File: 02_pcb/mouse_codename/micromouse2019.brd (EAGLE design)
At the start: 45 x 50 mm, 77 parts

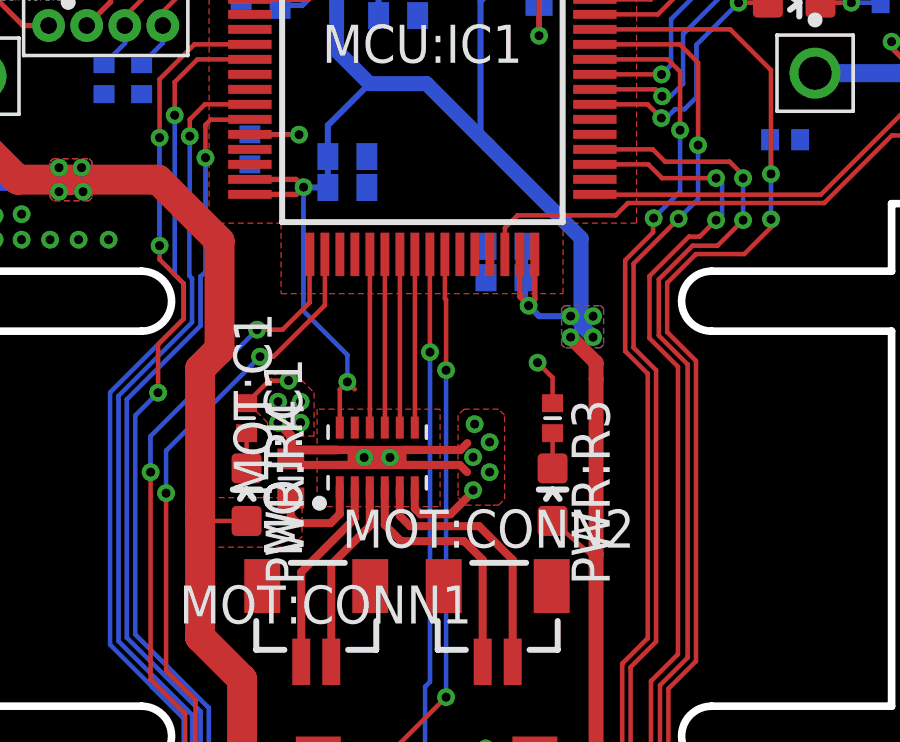
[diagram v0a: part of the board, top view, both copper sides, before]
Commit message: mot drv wire stub removed
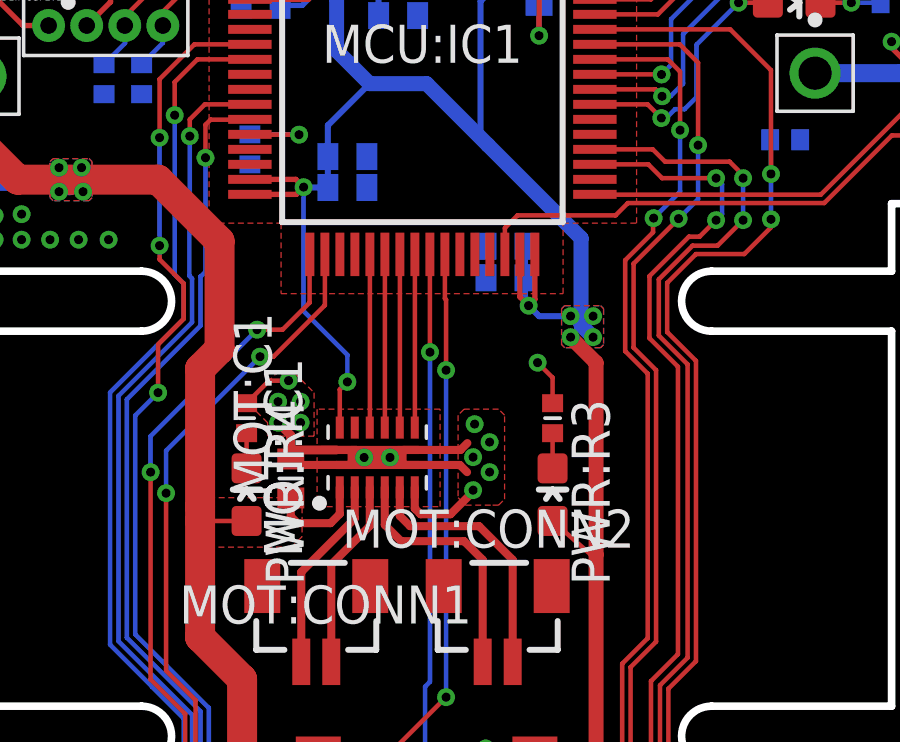
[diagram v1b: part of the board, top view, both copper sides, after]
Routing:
- net +3V3: track 165.8 -> 165.2 mm
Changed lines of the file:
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@@
 <drawing>
 <settings>
-<setting alwaysvectorfont="yes"/>
+<setting alwaysvectorfont="no"/>
 <setting verticaltext="up"/>
 </settings>
@@
 <contactref element="EPL:PORT1" pad="P3"/>
 <contactref element="PWR:LDO1" pad="1"/>
-<wire x1="20.106" y1="23.814" x2="19.86" y2="24.06" width="0.1524" layer="1"/>
 <wire x1="19.606" y1="22.5356" x2="19.606" y2="23.806" width="0.1524" layer="1"/>
 <wire x1="19.606" y1="23.806" x2="19.86" y2="24.06" width="0.1524" layer="1"/>
@@
 <wire x1="38.19" y1="4.73" x2="38.19" y2="3.71" width="0.1524" layer="16"/>
 <wire x1="38.19" y1="3.71" x2="38.2" y2="3.7" width="0.1524" layer="16"/>
-<wire x1="28.15" y1="18.3" x2="28.15" y2="24.15" width="0.5" layer="1"/>
+<wire x1="28.15" y1="18.3" x2="28.15" y2="24.7" width="0.5" layer="1"/>
 <wire x1="19.86" y1="24.06" x2="19.86" y2="24.96" width="0.1524" layer="16"/>
 <wire x1="19.86" y1="24.96" x2="18.4" y2="26.42" width="0.1524" layer="16"/>
@@
 <wire x1="16.61" y1="30.81" x2="18.14" y2="30.81" width="0.1778" layer="1"/>
 <wire x1="18.14" y1="30.81" x2="18.25" y2="30.7" width="0.1778" layer="1"/>
-<wire x1="18.25" y1="30.7" x2="18.4" y2="30.55" width="0.1778" layer="1"/>
 <wire x1="18.4" y1="26.42" x2="18.4" y2="30.55" width="0.1524" layer="16"/>
 <wire x1="18.4" y1="30.55" x2="18.25" y2="30.7" width="0.1778" layer="1"/>
@@
 </polygon>
 <wire x1="28.15" y1="24.7" x2="27.3" y2="25.55" width="0.5" layer="1"/>
-<wire x1="28.15" y1="24.15" x2="28.15" y2="24.7" width="0.5" layer="1"/>
 <wire x1="28.05" y1="25.55" x2="27.65" y2="25.95" width="0.5" layer="16"/>
 <wire x1="22.5" y1="34" x2="20.6" y2="34" width="0.5" layer="16"/>
@@
 <wire x1="18.773" y1="46.177" x2="18.773" y2="46.225" width="0.127" layer="16"/>
 <wire x1="18.773" y1="46.225" x2="18.775" y2="46.225" width="0.127" layer="16"/>
+<wire x1="27.65" y1="25.95" x2="28.05" y2="26.25" width="0" layer="19" extent="16-16"/>
+<wire x1="27.3" y1="26.25" x2="27.65" y2="25.95" width="0" layer="19" extent="16-16"/>
+<wire x1="27.3" y1="25.55" x2="27.65" y2="25.95" width="0" layer="19" extent="16-16"/>
 </signal>
 <signal name="VCC">

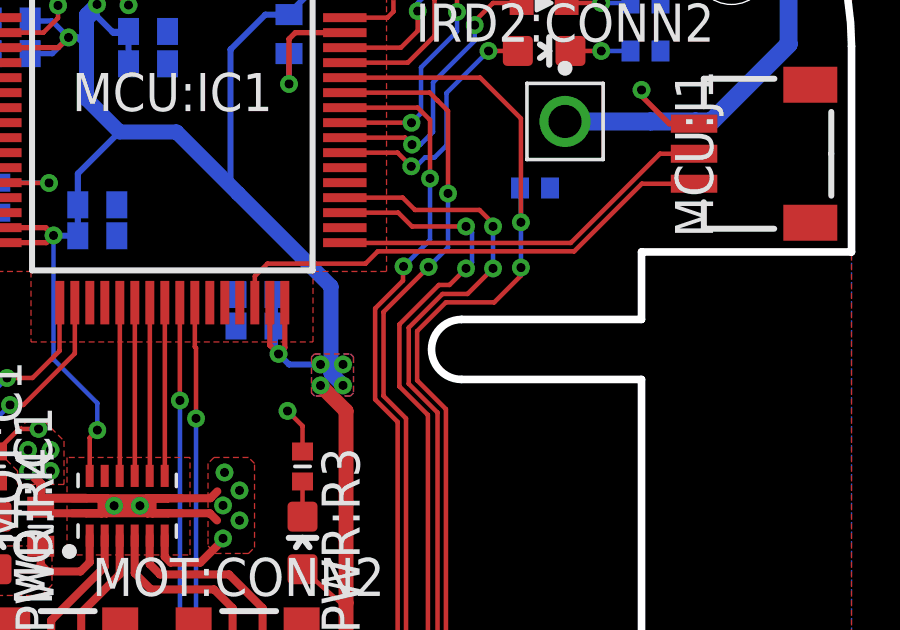
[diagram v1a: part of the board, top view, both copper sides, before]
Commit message: 100k resistor added to SWDIO for bidirectional managment
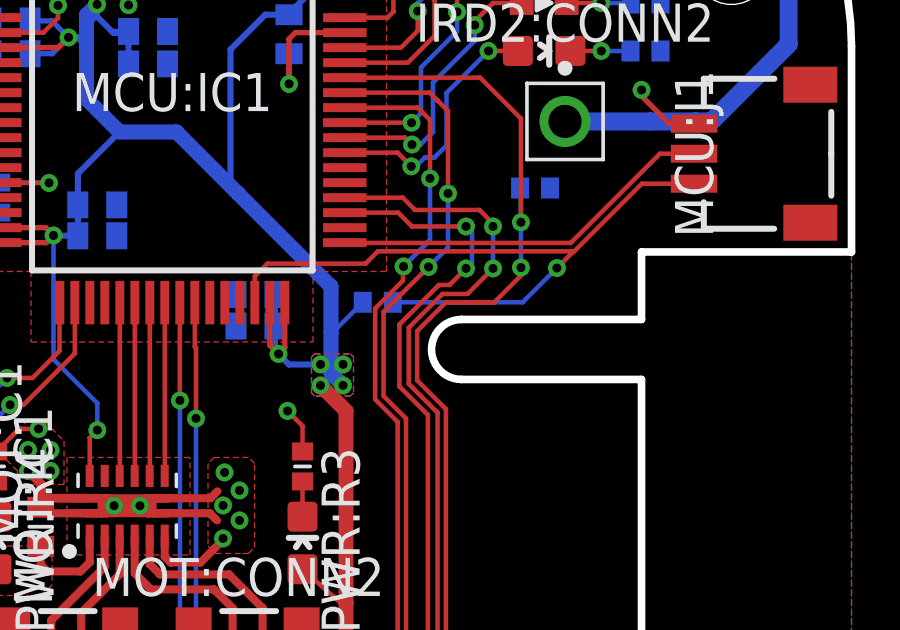
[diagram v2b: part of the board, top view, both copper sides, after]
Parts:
- added MCU:R10: 100k, rcl:R0402
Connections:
- net +3V3: now also MCU:R10.2
- net MCU:SWDIO: now also MCU:R10.1
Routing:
- net MCU:SWDIO: track 16.8 -> 23.5 mm, vias 0 -> 1
- net +3V3: track 165.2 -> 166.7 mm
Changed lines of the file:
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@@
 <attribute name="VALUE" x="20.701" y="-0.254" size="1.27" layer="27" align="top-center"/>
+</element>
+<element name="MCU:R10" library="rcl" library_urn="urn:adsk.eagle:library:334" package="R0402" package3d_urn="urn:adsk.eagle:package:23547/3" value="100k" x="29.21" y="28.321" smashed="yes" rot="MR0">
+<attribute name="NAME" x="29.845" y="28.956" size="1.27" layer="26" rot="MR0"/>
+<attribute name="SPICEPREFIX" value="R" x="29.21" y="28.321" size="1.778" layer="28" rot="MR0" display="off"/>
+<attribute name="VALUE" x="29.845" y="26.416" size="1.27" layer="28" rot="MR0"/>
 </element>
 </elements>
@@
 <wire x1="25.11" y1="29.19" x2="25.11" y2="28.31" width="0.1524" layer="1"/>
 <contactref element="MCU:IC1" pad="46"/>
+<contactref element="MCU:R10" pad="1"/>
+<wire x1="29.71" y1="28.321" x2="34.036" y2="28.321" width="0.1524" layer="16"/>
+<via x="35.179" y="29.464" extent="1-16" drill="0.3" diameter="0.6"/>
+<wire x1="35.179" y1="29.464" x2="35.7356" y2="30.0206" width="0.1524" layer="1"/>
+<wire x1="35.7356" y1="30.0206" x2="35.7557375" y2="30.0206" width="0.1524" layer="1"/>
+<wire x1="34.036" y1="28.321" x2="35.179" y2="29.464" width="0.1524" layer="16"/>
 </signal>
 <signal name="MCU:SWCLK">
@@
 <contactref element="CONN1" pad="1"/>
 <contactref element="CONN2" pad="1"/>
+<wire x1="26.25" y1="37.1" x2="22.2" y2="37.35" width="0" layer="19" extent="1-16"/>
 </signal>
 <signal name="+3V3">
@@
 <wire x1="22.5" y1="34" x2="20.6" y2="34" width="0.5" layer="16"/>
 <wire x1="20.6" y1="34" x2="19.5" y2="35.1" width="0.5" layer="16"/>
-<wire x1="27.65" y1="25.95" x2="27.65" y2="28.85" width="0.5" layer="16"/>
+<wire x1="27.65" y1="25.95" x2="27.65" y2="27.305" width="0.5" layer="16"/>
+<wire x1="27.65" y1="27.305" x2="27.65" y2="28.85" width="0.5" layer="16"/>
 <wire x1="27.65" y1="28.85" x2="24.55" y2="31.95" width="0.5" layer="16"/>
 <wire x1="24.55" y1="31.95" x2="22.5" y2="34" width="0.5" layer="16"/>
@@
 <wire x1="18.773" y1="46.177" x2="18.773" y2="46.225" width="0.127" layer="16"/>
 <wire x1="18.773" y1="46.225" x2="18.775" y2="46.225" width="0.127" layer="16"/>
-<wire x1="27.65" y1="25.95" x2="28.05" y2="26.25" width="0" layer="19" extent="16-16"/>
-<wire x1="27.3" y1="26.25" x2="27.65" y2="25.95" width="0" layer="19" extent="16-16"/>
-<wire x1="27.3" y1="25.55" x2="27.65" y2="25.95" width="0" layer="19" extent="16-16"/>
+<contactref element="MCU:R10" pad="2"/>
+<wire x1="28.71" y1="28.321" x2="27.694" y2="27.305" width="0.1524" layer="16"/>
+<wire x1="27.694" y1="27.305" x2="27.65" y2="27.305" width="0.1524" layer="16"/>
 </signal>
 <signal name="VCC">

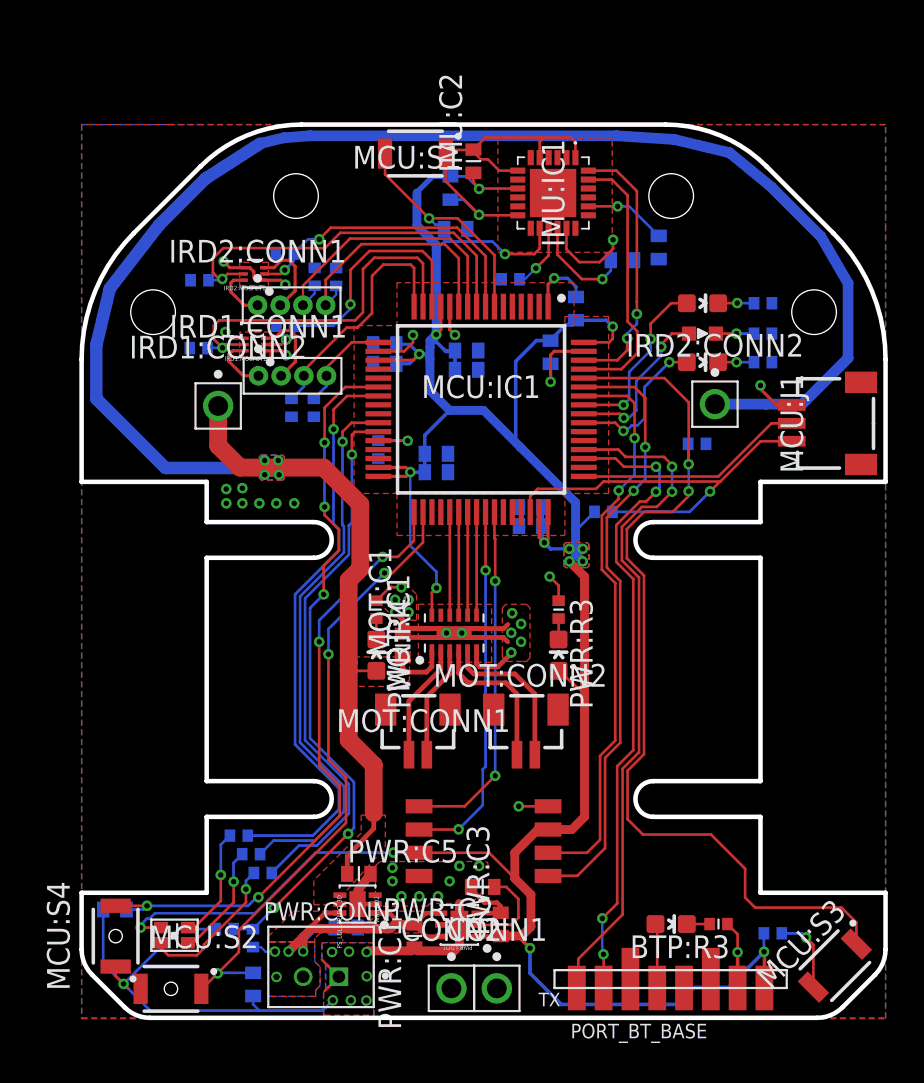
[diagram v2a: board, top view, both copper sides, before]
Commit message: tNames sized and placed to position
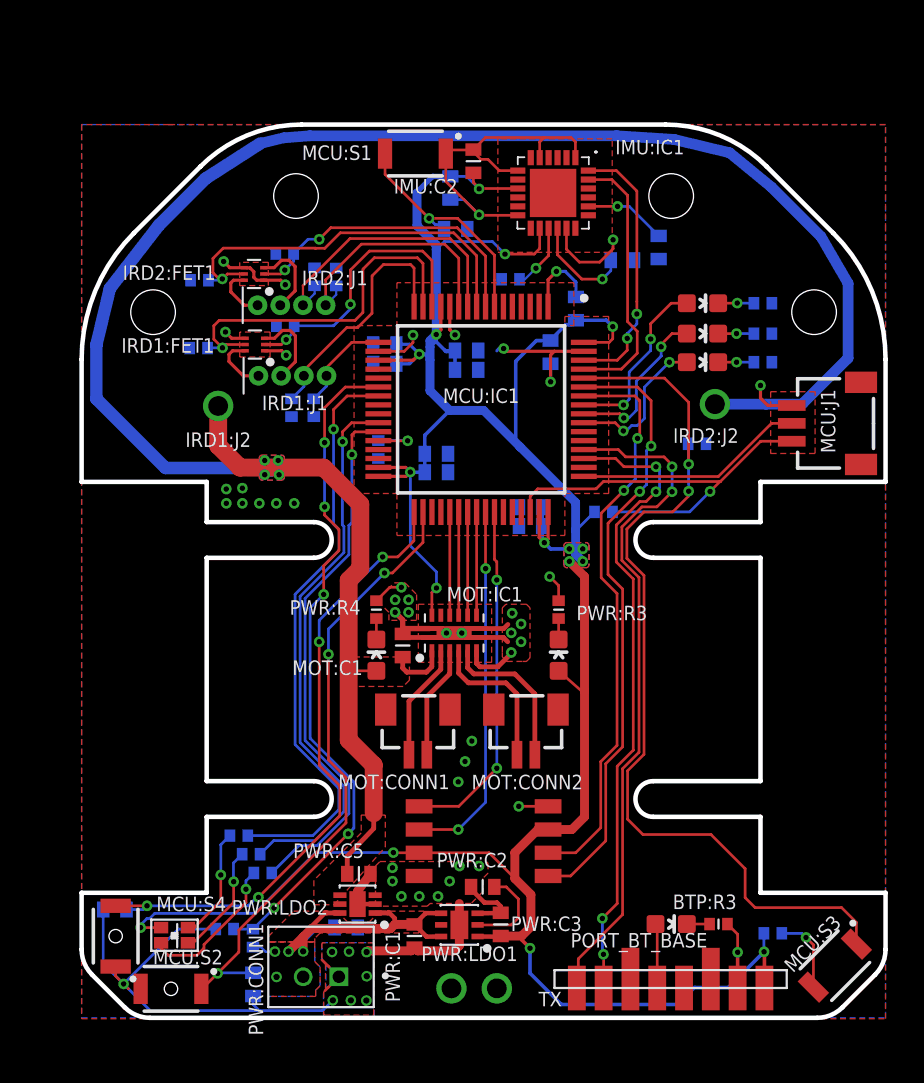
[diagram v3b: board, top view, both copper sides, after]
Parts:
- renumbered IRD1:CONN1 to IRD1:J1, IRD1:CONN2 to IRD1:J2, IRD1:MOSFET1 to IRD1:FET1, IRD2:CONN1 to IRD2:J1, IRD2:CONN2 to IRD2:J2, IRD2:MOSFET1 to IRD2:FET1
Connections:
- net ENC_LEFT_CHA: now also EPL:PORT1.P1, MCU:IC1.42; no longer EPL:PORT1.P2, MCU:IC1.41
- net ENC_LEFT_CHB: now also EPL:PORT1.P2, MCU:IC1.41; no longer EPL:PORT1.P1, MCU:IC1.42
- net ENC_RIGHT_CHA: now also EPR:PORT1.P1, MCU:IC1.59; no longer EPR:PORT1.P2, MCU:IC1.58
- net ENC_RIGHT_CHB: now also EPR:PORT1.P2, MCU:IC1.58; no longer EPR:PORT1.P1, MCU:IC1.59
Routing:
- net GND: track 119.8 -> 123.5 mm, vias 48 -> 52
- net ENC_RIGHT_CHA: track 32.1 -> 34.5 mm
- net ENC_RIGHT_CHB: track 34.3 -> 32.3 mm
- net ENC_LEFT_CHA: track 20.6 -> 19.6 mm
- net ENC_LEFT_CHB: track 19.7 -> 20.6 mm
- net MCU:V_BAT: track 3.73 -> 4.34 mm

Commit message: drc rule check ok
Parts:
- MCU:R1, MCU:R10: device rcl:R0402 -> 0-micromouse2019:R0402
- moved PWR:R1 1.06 mm to (8.56, 4.20)
- moved PWR:R2 1.05 mm to (6.99, 4.72)
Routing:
- net GND: track 123.5 -> 119.5 mm
- net V_BAT_LEVEL: track 38.1 -> 39.3 mm
- net PWR:V_BAT_IN: track 19.7 -> 20.6 mm

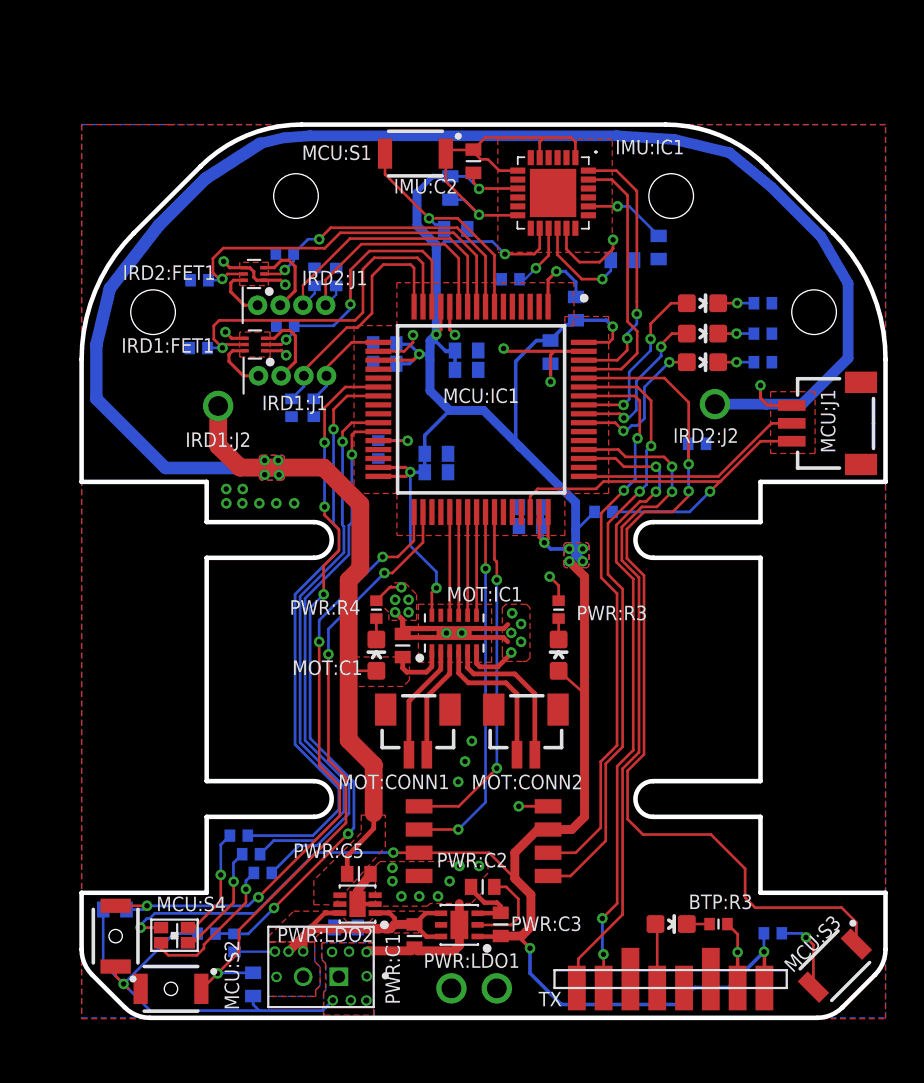
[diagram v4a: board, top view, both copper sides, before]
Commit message: FET thermal ground added & LDOs & FET variant names corrected
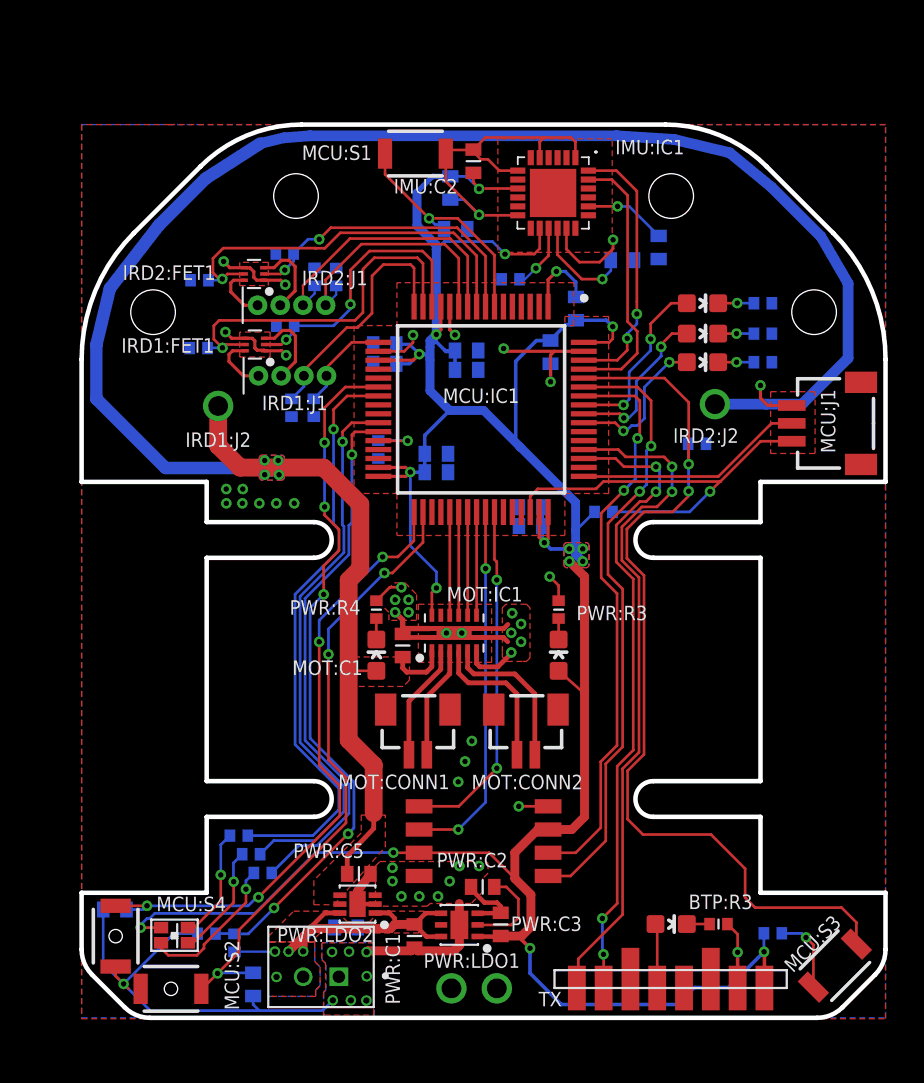
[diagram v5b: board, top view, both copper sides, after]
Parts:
- IRD1:FET1, IRD2:FET1: value FET_DMN2990UDJ-7MOSFET_SOT964 -> FET_DMN2990UDJ-7
- PWR:LDO1: value PS_TPS7353D -> PS_TPS735DRVT
- PWR:LDO2: value PS_LDL112LDO_3D -> PS_LDL112PU
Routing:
- net GND: track 119.5 -> 121.1 mm

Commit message: mpu 6050 library fixed
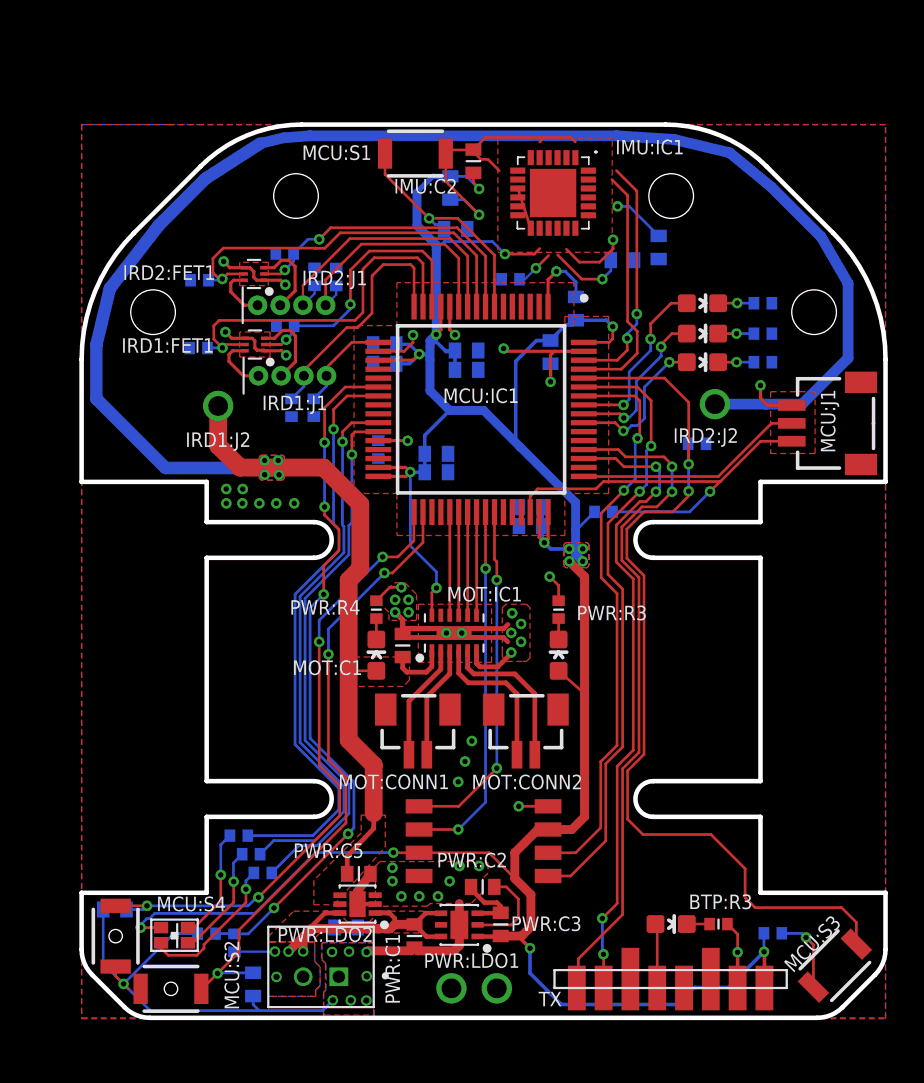
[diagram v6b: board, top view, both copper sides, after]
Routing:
- net GND: track 121.1 -> 112.0 mm
- net IMU:CPOUT: track 4.62 -> 2.99 mm
- net SDA: track 15.0 -> 13.4 mm
- net IMU:AD0: track 3.71 -> 2.18 mm
- net IMU:REGOUT: track 5.82 -> 4.33 mm
- net SCL: track 15.0 -> 13.7 mm
- net +3V3: track 166.7 -> 165.7 mm
